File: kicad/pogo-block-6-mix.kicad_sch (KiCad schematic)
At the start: 34 parts, among them J27 BP3_L_OUT, J28 BP3_R_OUT, U27 TL072, U46 TL072, U47 TL072, U48 TL072

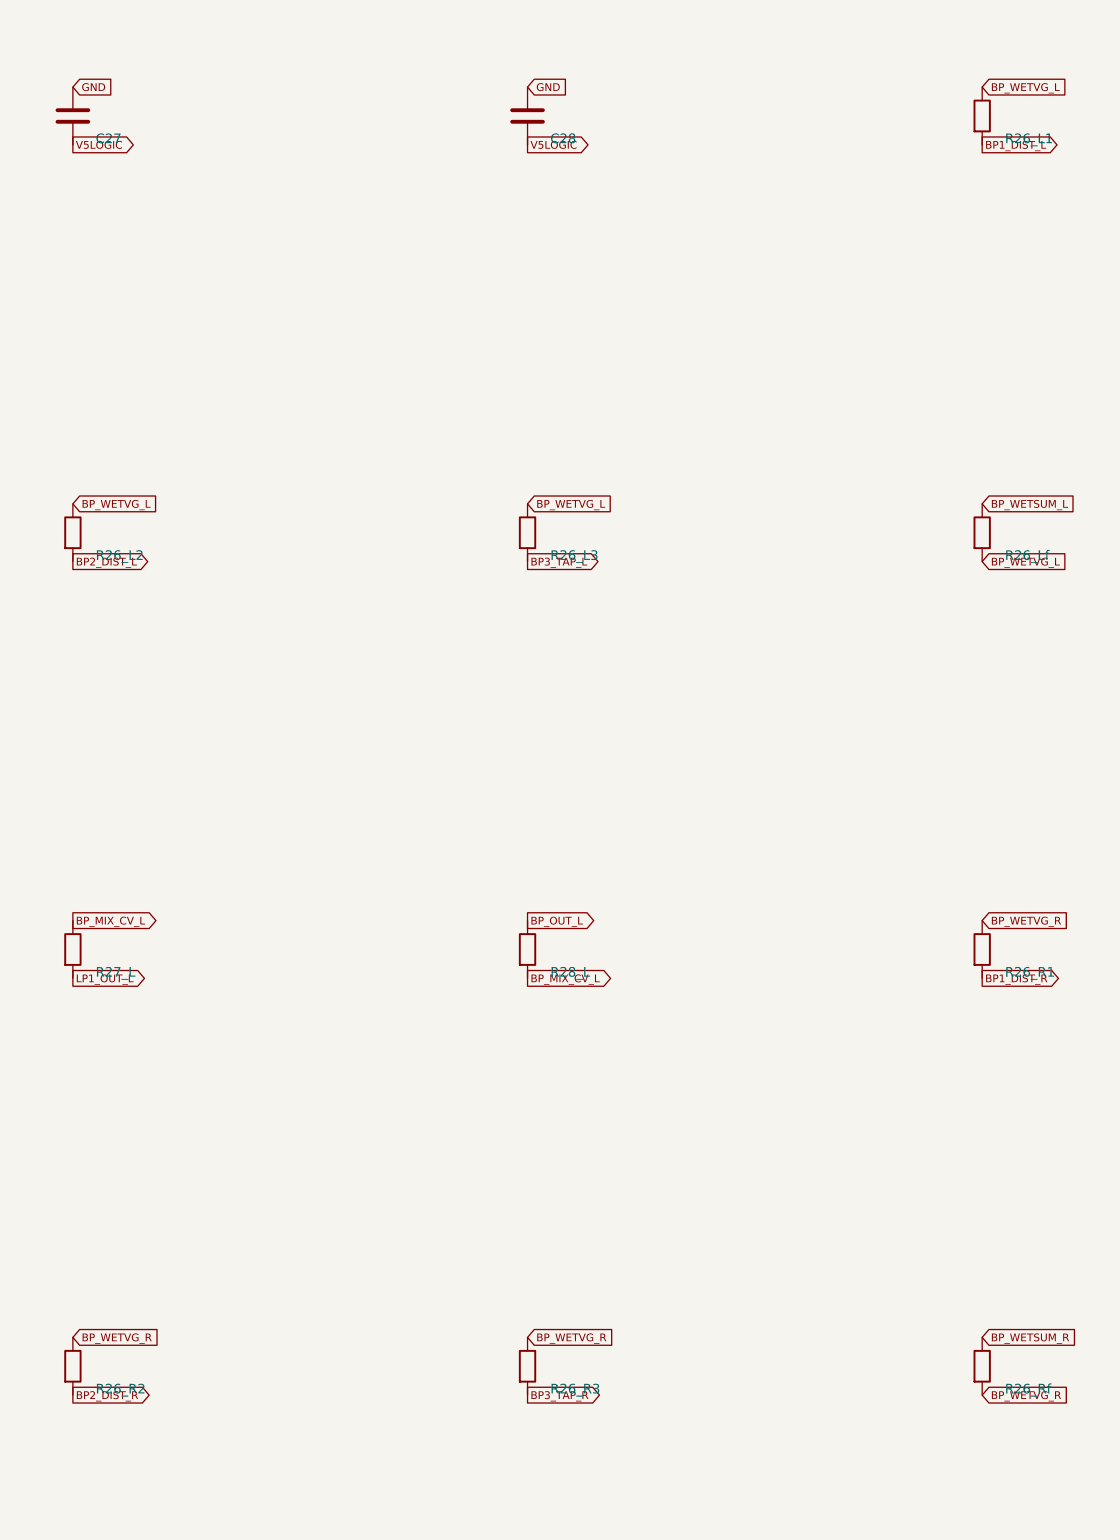
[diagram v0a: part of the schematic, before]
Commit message: 0018: block-6 stage 2 - distortion BEFORE bandpass (0017 reorder)
The core 0017 change: flip the per-band order from SVF->DIST to DIST->SVF to
match the plugin (Pogo.cpp:443-451). Realized as a net re-point across the 7
split sections (no part changes):
  LP1_OUT / BP3IN  ->  distN (R18/R20/R22 distortion inputs)
                   ->  mux out (BPn_DISTOUT)  ->  svfN SUM_AMP (R13)
                   ->  SVF v1 buffer (BPn_BANDOUT / BP3_TAP)  ->  mix wet summer
- BP1/BP2 take the LP1 band; BP3 takes BP3IN (the ALT/LP1 selector, stage 3).
- BP3 OUT tap now taken post-bandpass (BP3_TAP = svf3 v1), matching the plugin
  (prevOut[2]); block-B keeps the BP3_TAP net name (no block-B change).
- spec §1/§2 updated: signal order, DIST knob, ALT path (through-VCA/BP3-only),
  BP3 tap point.

Boundary symmetry verified for all re-pointed nets; all 5 --check gates +
parity green.

https://claude.ai/code/session_013jFXG5oeMVSYP7iRpwGvtQ
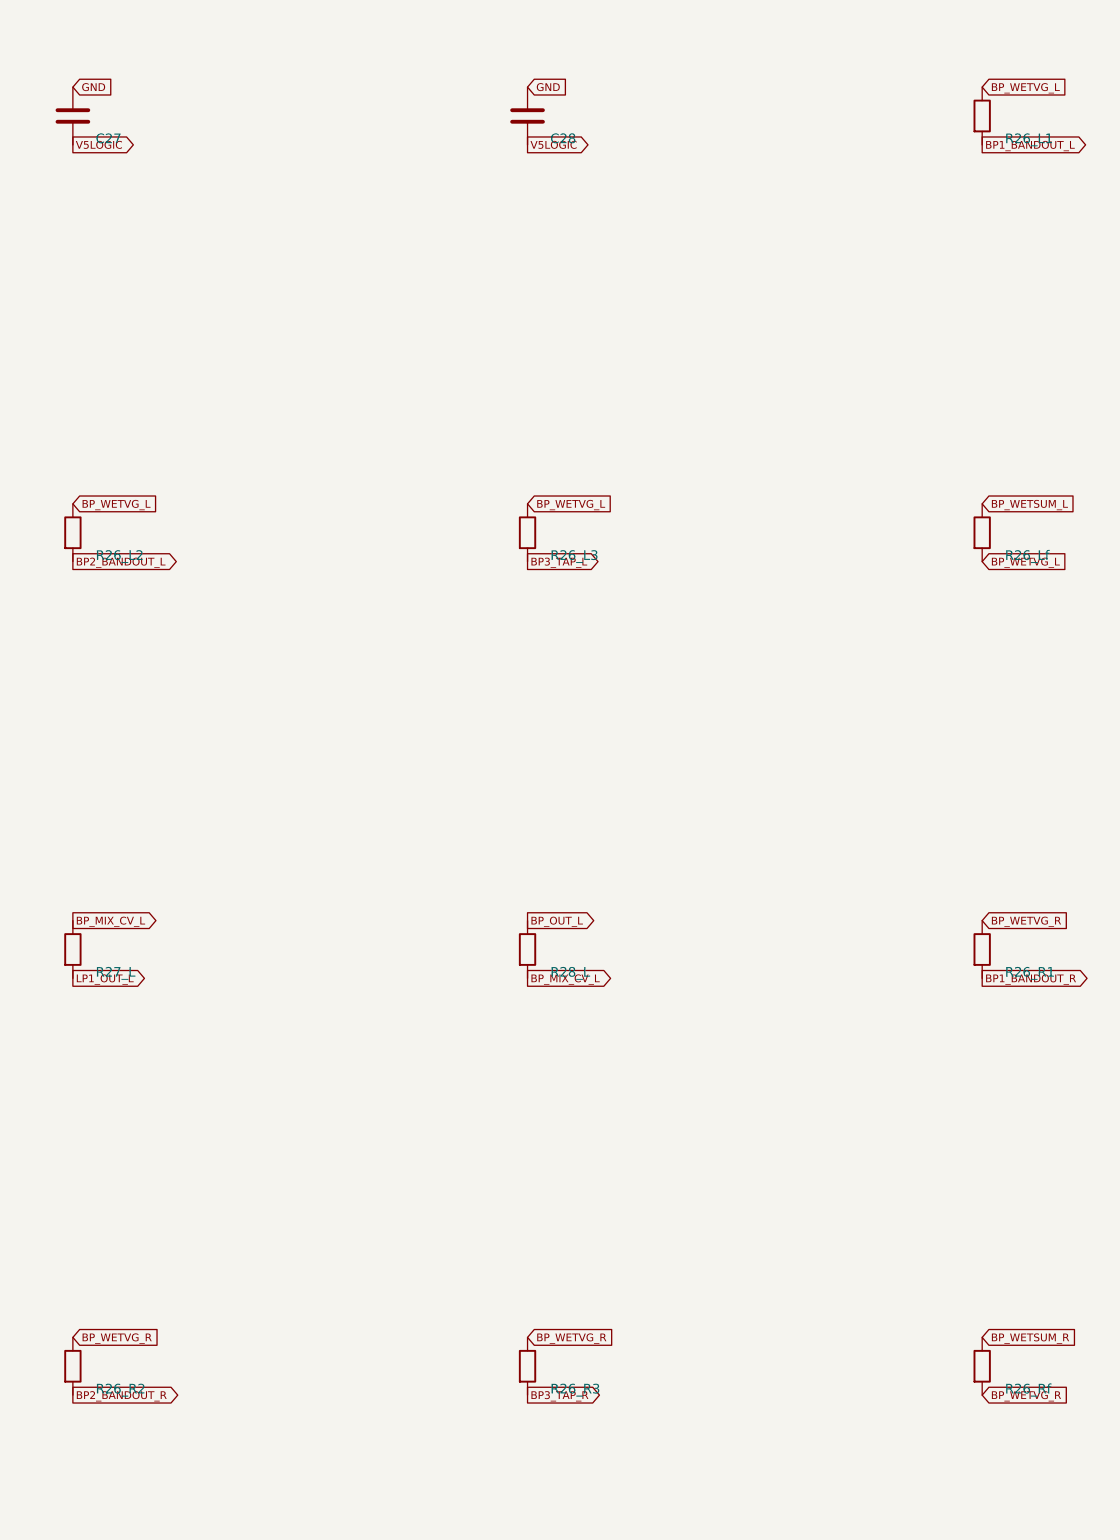
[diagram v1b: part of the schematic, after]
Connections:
- net BP1_DIST_L renamed BP1_BANDOUT_L
- net BP1_DIST_R renamed BP1_BANDOUT_R
- net BP2_DIST_L renamed BP2_BANDOUT_L
- net BP2_DIST_R renamed BP2_BANDOUT_R
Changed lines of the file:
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@@
   (effects (font (size 1.016 1.016)) (justify left))
 )
-(global_label "BP1_DIST_L"
+(global_label "BP1_BANDOUT_L"
   (shape output)
   (at 160.000 373.810 0)
   (effects (font (size 1.016 1.016)) (justify left))
 )
-(global_label "BP1_DIST_R"
+(global_label "BP1_BANDOUT_R"
   (shape output)
   (at 160.000 483.810 0)
   (effects (font (size 1.016 1.016)) (justify left))
 )
-(global_label "BP2_DIST_L"
+(global_label "BP2_BANDOUT_L"
   (shape output)
   (at 40.000 428.810 0)
   (effects (font (size 1.016 1.016)) (justify left))
 )
-(global_label "BP2_DIST_R"
+(global_label "BP2_BANDOUT_R"
   (shape output)
   (at 40.000 538.810 0)

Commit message: 0018: block-6 stage 4 - per-band BP TILT (summer+inverter/band)
The per-band tilt was entirely unbuilt (the panel BP1/2/3 TILT knobs had no
hardware control component at all, and only the master tilt was wired). Build
it to match the plugin's groupTiltV[i] = BPn_TILT_PARAM + CV*0.22:
- Per band (svf1/2/3): +1 TL072 (U82-84) as an inverting summer + inverter.
  Summer combines master tilt (BP_TILT_CV, 100k) + the per-band TILT knob
  (RV48-50 bipolar, 100k) + the per-band TILT CV (MOD_BPn_TILT from block-3,
  470k -> x0.213 ~= the plugin's x0.22). -total feeds the R expo base; the
  inverter's +total feeds the L expo base.
- Re-pointed R127_nL/R from the old shared master tilt onto the per-band
  +/-total; removed the shared master inverter (U27-A) so BP_NTILT is gone
  everywhere; U27 kept for its still-live polarity-restore half.
- New parts: U82-84, RV48-50, R135-152, C119-124. New boundary MOD_BPn_TILT.
- Exact tilt-range reference/scaling is Phase-3R (noted), like block-6's other
  calibration items.

All 5 --check gates + parity green; boundary symmetry verified (BP_NTILT gone,
MOD_BPn_TILT symmetric). G5/G6a.

https://claude.ai/code/session_013jFXG5oeMVSYP7iRpwGvtQ
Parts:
- removed J27: BP3_L_OUT, POGO_Connector_Audio:Jack_3.5mm_QingPu_WQP-PJ398SM_Vertical_CircularHoles, symbol Device:Audio_Jack_3.5mm_SwitchT
- removed J28: BP3_R_OUT, POGO_Connector_Audio:Jack_3.5mm_QingPu_WQP-PJ398SM_Vertical_CircularHoles, symbol Device:Audio_Jack_3.5mm_SwitchT
- C27: renamed from R29; value 1k -> 10uF; symbol Device:R -> Device:C
- C28: renamed from D7; value BZX84C5V1 -> 100nF; footprint POGO_Package_TO_SOT_SMD:SOT-23 -> (none); symbol Diode:D_Zener -> Device:C
- D7: renamed from R17_fb; value 100k -> BZX84C5V1; footprint (none) -> POGO_Package_TO_SOT_SMD:SOT-23; symbol Device:R -> Diode:D_Zener
- J27: renamed from R27_R; value 100k -> BP3_L_OUT; footprint (none) -> POGO_Connector_Audio:Jack_3.5mm_QingPu_WQP-PJ398SM_Vertical_CircularHoles; symbol Device:R -> Device:Audio_Jack_3.5mm_SwitchT
- J28: renamed from R28_R; value 100k -> BP3_R_OUT; footprint (none) -> POGO_Connector_Audio:Jack_3.5mm_QingPu_WQP-PJ398SM_Vertical_CircularHoles; symbol Device:R -> Device:Audio_Jack_3.5mm_SwitchT
- R26_L1: renamed from C27; value 10uF -> 33k; symbol Device:C -> Device:R
- R26_L2: renamed from C28; value 100nF -> 33k; symbol Device:C -> Device:R
- R26_R1: renamed from R27_L; value 100k -> 33k
- R26_R2: renamed from R28_L; value 100k -> 33k
- R27_L: renamed from R26_L3; value 33k -> 100k
- R27_R: renamed from R26_R3; value 33k -> 100k
- R28_L: renamed from R26_Lf; value 33k -> 100k
- R28_R: renamed from R26_Rf; value 33k -> 100k
- R29: renamed from R17_in; value 100k -> 1k
- renumbered R16_fb to R17_fb, R16_in to R17_in, R26_L1 to R26_L3, R26_L2 to R26_Lf, R26_R1 to R26_R3, R26_R2 to R26_Rf
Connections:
- net BP_TILT_CV is gone; now on net BP_OUT_L: R17_in.2
- net +12V: now also R29.2; no longer C27.2
- net BP1_BANDOUT_L: now also R26_L1.2; no longer R26_L3.2
- net BP1_BANDOUT_R: now also R26_R1.2; no longer R26_R3.2
- net BP2_BANDOUT_L: now also R26_L2.2; no longer R26_Lf.2
- net BP2_BANDOUT_R: now also R26_R2.2; no longer R26_Rf.2
- net BP3_L_OUT: now also J27.1 (T)
- net BP3_R_OUT: now also J28.1 (T)
- net BP3_TAP_L: now also R26_L3.2; no longer R27_L.2
- net BP3_TAP_R: now also R26_R3.2; no longer R27_R.2
- net BP_MIX_CV_L: now also R27_L.1, R28_L.2; no longer R26_R1.1, R26_R2.2
- net BP_MIX_CV_R: now also R27_R.1, R28_R.2; no longer J27.1, J28.2
- net BP_OUT_L: now also R28_L.1; no longer R26_R2.1, R29.2
- net BP_OUT_R: now also R28_R.1; no longer J28.1
- net BP_POLRESTORE_L: now also R17_fb.1; no longer D7.1
- net BP_POLVG_L: now also R17_fb.2, R17_in.1; no longer D7.2, R29.1
- net BP_WETSUM_L: now also R26_Lf.1; no longer R28_L.1
- net BP_WETSUM_R: now also R26_Rf.1; no longer R28_R.1
- net BP_WETVG_L: now also R26_L1.1, R26_L2.1, R26_Lf.2; no longer R26_Lf.1, R27_L.1, R28_L.2
- net BP_WETVG_R: now also R26_R1.1, R26_R2.1, R26_Rf.2; no longer R26_Rf.1, R27_R.1, R28_R.2
- net GND: now also C27.1, C28.1, D7.3 (K), J27.2 (S), J28.2 (S); no longer C28.3 (K), R26_L1.1, R26_L2.1
- net LP1_OUT_L: now also R27_L.2; no longer R26_R1.2
- net LP1_OUT_R: now also R27_R.2; no longer J27.2
- net V5LOGIC: now also C27.2, C28.2, D7.1 (A), R29.1; no longer C27.1, C28.1 (A), R26_L1.2, R26_L2.2
- net BP_NTILT renamed U27A_UNUSED
- net U27A_UNUSED: now also U27.3 (In+); no longer R17_fb.1
- removed net BP_TILT_INVN: R17_fb.2, R17_in.1, U27.3 (In+)

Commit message: 0018: block-6 stage 7 - two independent dry/wet scalers (mix)
Final block-6 stage: rework the mix to the plugin's two-scaler output
bpOut = bandL*BP_BYPASS + wetSum*BP_WET (two independent 0-1 levels, not a
crossfade):
- Wet 3-band sum (U46/47-A, inv) re-inverted by U48 (G=-1) -> BP_WETPOS (+bands).
- BYPASS dual-gang pot (RV30 L / RV58 R) attenuates dry LP1 band; new WET
  dual-gang pot (RV57 L / RV59 R) attenuates BP_WETPOS; both wipers sum in the
  final inverting summer (U46/47-B); output polarity restore per channel
  (U27-B = L existing, U27-A = R reused) -> BP_OUT.
- Polarity arranged so wet ADDS with dry at BP_OUT (accounts for the Stage-5
  DRIVE-VCA I/V inversion); exact phase-vs-freq and pot tapers are Phase-3R.
- Removed the old single-pot crossfade (R27, BP_MIX_CV, BP_WETPOS-as-boundary);
  +RV57/58/59, R214-223. spec §2 BP_MIX flag marked RESOLVED.

block-6 now fully aligned (split + 7 stages). All 5 --check gates + parity
green; BP_OUT_L/R -> block-7 confirmed.

https://claude.ai/code/session_013jFXG5oeMVSYP7iRpwGvtQ
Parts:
- added J27: BP3_L_OUT, POGO_Connector_Audio:Jack_3.5mm_QingPu_WQP-PJ398SM_Vertical_CircularHoles, symbol Device:Audio_Jack_3.5mm_SwitchT
- added J28: BP3_R_OUT, POGO_Connector_Audio:Jack_3.5mm_QingPu_WQP-PJ398SM_Vertical_CircularHoles, symbol Device:Audio_Jack_3.5mm_SwitchT
- added R214, R215, R216, R217, R218, R219, R220, R221, R222, R223: 100k, symbol Device:R
- R26_R1: renamed from R28_L; value 100k -> 33k
- R28_R: renamed from R26_Rf; value 33k -> 100k
- RV30: renamed from R27_R; value 100k -> BP_BYPASS_L; footprint (none) -> POGO_Potentiometer_THT:Potentiometer_Alpha_RD901F-40-00D_Single_Vertical_CircularHoles; symbol Device:R -> Device:R_POT
- RV57: renamed from J27; value BP3_L_OUT -> BP_WET_L; footprint POGO_Connector_Audio:Jack_3.5mm_QingPu_WQP-PJ398SM_Vertical_CircularHoles -> POGO_Potentiometer_THT:Potentiometer_Alpha_RD901F-40-00D_Single_Vertical_CircularHoles; symbol Device:Audio_Jack_3.5mm_SwitchT -> Device:R_POT
- RV58: renamed from R28_R; value 100k -> BP_BYPASS_R; footprint (none) -> POGO_Potentiometer_THT:Potentiometer_Alpha_RD901F-40-00D_Single_Vertical_CircularHoles; symbol Device:R -> Device:R_POT
- RV59: renamed from J28; value BP3_R_OUT -> BP_WET_R; footprint POGO_Connector_Audio:Jack_3.5mm_QingPu_WQP-PJ398SM_Vertical_CircularHoles -> POGO_Potentiometer_THT:Potentiometer_Alpha_RD901F-40-00D_Single_Vertical_CircularHoles; symbol Device:Audio_Jack_3.5mm_SwitchT -> Device:R_POT
- renumbered R26_R1 to R26_R2, R26_R2 to R26_R3, R26_R3 to R26_Rf, R27_L to R28_L
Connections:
- net BP_POLRESTORE_L is gone; now on net BP_OUT_L: R17_fb.1, U27.7 (Out)
- net BP1_BANDOUT_R: now also R26_R1.2; no longer R26_R2.2
- net BP2_BANDOUT_R: now also R26_R2.2; no longer R26_R3.2
- net BP3_L_OUT: now also J27.1 (T); no longer RV57.1 (T)
- net BP3_R_OUT: now also J28.1 (T); no longer RV59.1 (T)
- net BP3_TAP_R: now also R26_R3.2; no longer R26_Rf.2
- net BP_OUT_L: no longer R17_in.2, R26_R1.1, U46.7 (Out)
- net BP_OUT_R: now also U27.1 (Out), R223.1; no longer RV58.1, U47.7 (Out)
- net BP_WETPOS_L: now also RV57.1, R215.1; no longer U48.3 (In+)
- net BP_WETPOS_R: now also RV59.1, R217.1; no longer U48.5 (In+)
- net BP_WETSUM_L: now also R214.2; no longer U48.2 (In-)
- net BP_WETSUM_R: now also R26_Rf.1, R216.2; no longer R28_R.1, U48.6 (In-)
- net BP_WETVG_R: now also R26_R1.1, R26_Rf.2; no longer R26_Rf.1, R28_R.2
- net GND: now also RV30.3, RV57.3, RV58.3, RV59.3, U48.2 (In-), U48.6 (In-), J27.2 (S), J28.2 (S); no longer RV57.2 (S), RV59.2 (S)
- net LP1_OUT_L: now also RV30.1; no longer R28_L.2
- net LP1_OUT_R: now also RV58.1; no longer RV30.2
- removed net BP_MIX_CV_L: R26_R1.2, R28_L.1, U46.5 (In+)
- removed net BP_MIX_CV_R: RV30.1, RV58.2, U47.5 (In+)
- net U27A_UNUSED renamed BP_POLVG_R
- net BP_POLVG_R: now also R222.1, R223.2; no longer U27.1 (Out)
- new net BP_BYPASS_W_L: R218.2, RV30.2 (Wiper)
- new net BP_BYPASS_W_R: R220.2, RV58.2 (Wiper)
- new net BP_MIXOUT_L: R17_in.2, R28_L.1, U46.7 (Out)
- new net BP_MIXOUT_R: R222.2, R28_R.1, U47.7 (Out)
- new net BP_MIX_VG_L: R218.1, R219.1, R28_L.2, U46.5 (In+)
- new net BP_MIX_VG_R: R220.1, R221.1, R28_R.2, U47.5 (In+)
- new net BP_WETINV_L: R214.1, R215.2, U48.3 (In+)
- new net BP_WETINV_R: R216.1, R217.2, U48.5 (In+)
- new net BP_WET_W_L: R219.2, RV57.2 (Wiper)
- new net BP_WET_W_R: R221.2, RV59.2 (Wiper)

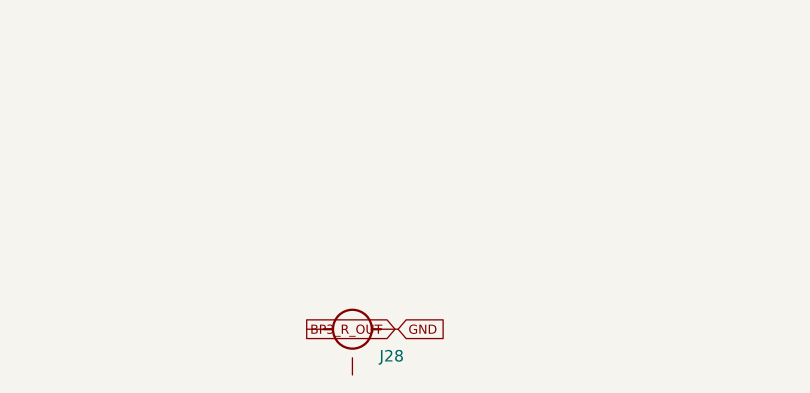
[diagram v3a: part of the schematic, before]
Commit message: 0018: block-B output buffers aligned to plugin (BP3_R normal + hygiene)
Final block. Adversarial review confirmed MAIN outputs faithful (non-inverting
unity followers, 1k series, +-11V via TL072 swing = plugin clamp, like block-A)
and the BP3 tap point correct (svf3 v1, post-bandpass/pre-mix). One real gap:
- BP3_R OUTPUT NORMALLING added: the plugin outputs BP3_L when the BP3_R jack
  is unpatched (Pogo.cpp:498-499). Wired J28.3 (switch lug) -> BP3_L_OUT in
  block-6-mix (which owns the BP3 jacks): BP3_L_OUT: [J27.1, J28.3], J28.3
  removed from no_connect. Mirrors block-A's L->R input normal.
- Renumbered block-B R37 -> R224 to clear the cross-block R37 collision with
  block-3's CV-protection resistors.
- Lifted §2/§3 STALE banners; fixed aux-unity-buffer refs (.svg/.md); noted the
  LFO output resistors are block-2 (utility), editorial in block-B.

All 10 blocks now aligned to the locked plugin. All 5 --check gates + parity green.

https://claude.ai/code/session_013jFXG5oeMVSYP7iRpwGvtQ
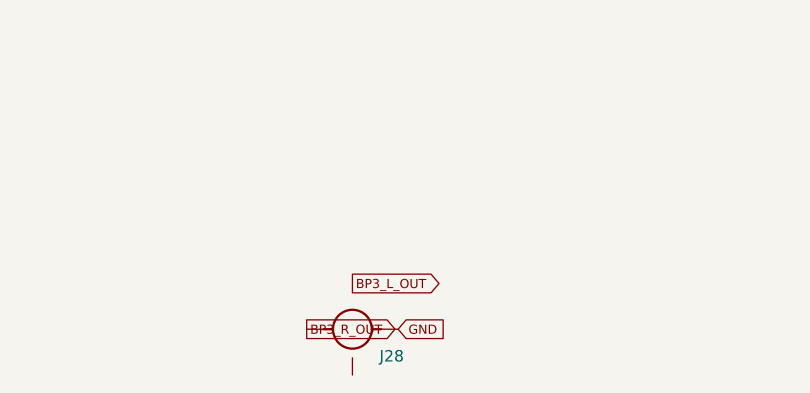
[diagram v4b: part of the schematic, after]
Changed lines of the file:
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@@
+  (effects (font (size 1.016 1.016)) (justify left))
+)
+(global_label "BP3_L_OUT"
+  (shape output)
+  (at 100.000 804.920 0)
   (effects (font (size 1.016 1.016)) (justify left))
 )
